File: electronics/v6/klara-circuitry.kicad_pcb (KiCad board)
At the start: 2 copper layers, 70 x 84 mm, 15 parts, among them J1 Pin header, U1 MCP1700-3302E, U3 ATtiny85

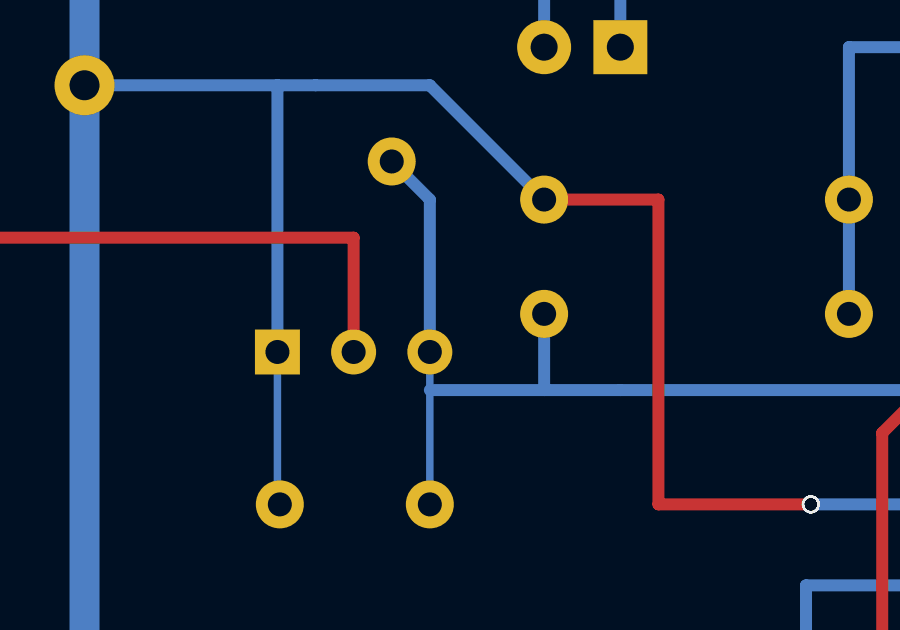
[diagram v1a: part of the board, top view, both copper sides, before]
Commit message: circuit d'oh: measure supercap voltage, not regulator output
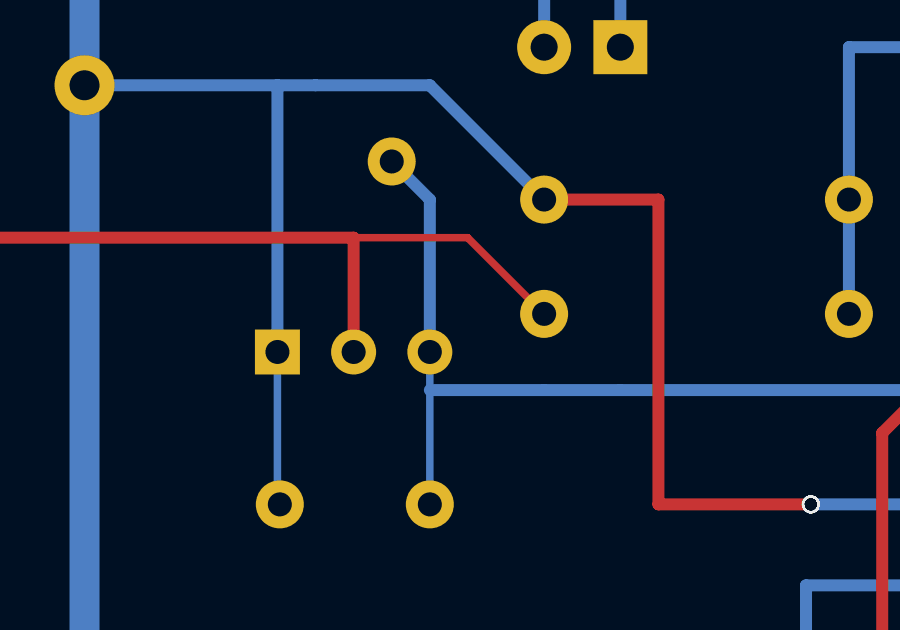
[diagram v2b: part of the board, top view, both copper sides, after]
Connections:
- R2 pad 1: Net-(C2-Pad1) -> Net-(CS1-Pad1)
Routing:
- net Net-(CS1-Pad1): track 64.6 -> 72.0 mm
- net Net-(C2-Pad1): track 73.5 -> 71.0 mm
